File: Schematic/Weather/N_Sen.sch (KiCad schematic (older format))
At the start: 27 parts, among them J2 3_Way_Wire, J3 3_Way_Wire, Q1 BSS138, Q2 AO3401, Q3 AO3401, U5 LM321

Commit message: more changes
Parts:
- renumbered C4 to C1, H1 to H3, H2 to H4, H3 to H5, H4 to H6, J3 to J10, J2 to J9, R3 to R1, R12 to R10, R13 to R11, R14 to R12, R15 to R13, R16 to R14, R4 to R2, R5 to R3, R6 to R4, R7 to R5, R8 to R6, R9 to R7, R10 to R8, R11 to R9, U5 to U4
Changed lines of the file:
@@
 $Descr A4 11693 8268
 encoding utf-8
-Sheet 9 14
+Sheet 9 15
 Title ""
 Date ""
@@
 $EndComp
 $Comp
-L Amplifier_Operational:LM321 U5
+L Amplifier_Operational:LM321 U4
 U 1 1 5C8F90C7
 P 6050 2150
-F 0 "U5" H 6050 2631 50  0000 C CNN
+F 0 "U4" H 6050 2631 50  0000 C CNN
 F 1 "LM321" H 6050 2540 50  0000 C CNN
 F 2 "Package_TO_SOT_SMD:SOT-23-5" H 6050 2150 50  0001 C CNN
@@
 $EndComp
 $Comp
-L Device:R R3
+L Device:R R1
 U 1 1 5C90C2DD
 P 5450 4800
-F 0 "R3" V 5243 4800 50  0000 C CNN
+F 0 "R1" V 5243 4800 50  0000 C CNN
 F 1 "2.2K" V 5334 4800 50  0000 C CNN
 F 2 "Resistor_THT:R_Axial_DIN0204_L3.6mm_D1.6mm_P2.54mm_Vertical" V 5380 4800 50  0001 C CNN
@@
 $EndComp
 $Comp
-L Device:R R6
+L Device:R R4
 U 1 1 5C90E169
 P 5850 5250
-F 0 "R6" H 5780 5204 50  0000 R CNN
+F 0 "R4" H 5780 5204 50  0000 R CNN
 F 1 "5.1K" H 5780 5295 50  0000 R CNN
 F 2 "Resistor_THT:R_Axial_DIN0204_L3.6mm_D1.6mm_P2.54mm_Vertical" V 5780 5250 50  0001 C CNN
@@
 $EndComp
 $Comp
-L Device:R R14
+L Device:R R12
 U 1 1 5C90F143
 P 7350 4900
-F 0 "R14" H 7420 4946 50  0000 L CNN
+F 0 "R12" H 7420 4946 50  0000 L CNN
 F 1 "680" H 7420 4855 50  0000 L CNN
 F 2 "Resistor_THT:R_Axial_DIN0204_L3.6mm_D1.6mm_P2.54mm_Vertical" V 7280 4900 50  0001 C CNN
@@
 $EndComp
 $Comp
-L Device:R R12
+L Device:R R10
 U 1 1 5C9100FA
 P 7050 3900
-F 0 "R12" H 7120 3946 50  0000 L CNN
+F 0 "R10" H 7120 3946 50  0000 L CNN
 F 1 "20K" H 7120 3855 50  0000 L CNN
 F 2 "Resistor_THT:R_Axial_DIN0204_L3.6mm_D1.6mm_P2.54mm_Vertical" V 6980 3900 50  0001 C CNN
@@
 $EndComp
 $Comp
-L Device:R R8
+L Device:R R6
 U 1 1 5C913744
 P 6300 4150
-F 0 "R8" H 6370 4196 50  0000 L CNN
+F 0 "R6" H 6370 4196 50  0000 L CNN
 F 1 "10K" H 6370 4105 50  0000 L CNN
 F 2 "Resistor_THT:R_Axial_DIN0204_L3.6mm_D1.6mm_P2.54mm_Vertical" V 6230 4150 50  0001 C CNN
@@
 $EndComp
 $Comp
-L Device:R R5
+L Device:R R3
 U 1 1 5C91429E
 P 5750 3700
-F 0 "R5" H 5820 3746 50  0000 L CNN
+F 0 "R3" H 5820 3746 50  0000 L CNN
 F 1 "2.2k" H 5820 3655 50  0000 L CNN
 F 2 "Resistor_THT:R_Axial_DIN0204_L3.6mm_D1.6mm_P2.54mm_Vertical" V 5680 3700 50  0001 C CNN
@@
 $EndComp
 $Comp
-L Device:R R9
+L Device:R R7
 U 1 1 5C919740
 P 6400 1700
-F 0 "R9" H 6470 1746 50  0000 L CNN
+F 0 "R7" H 6470 1746 50  0000 L CNN
 F 1 "4.7K" H 6470 1655 50  0000 L CNN
 F 2 "Resistor_THT:R_Axial_DIN0204_L3.6mm_D1.6mm_P2.54mm_Vertical" V 6330 1700 50  0001 C CNN
@@
 $EndComp
 $Comp
-L Device:R R4
+L Device:R R2
 U 1 1 5C902560
 P 5500 2150
-F 0 "R4" V 5293 2150 50  0000 C CNN
+F 0 "R2" V 5293 2150 50  0000 C CNN
 F 1 "4.7K" V 5384 2150 50  0000 C CNN
 F 2 "Resistor_THT:R_Axial_DIN0204_L3.6mm_D1.6mm_P2.54mm_Vertical" V 5430 2150 50  0001 C CNN
@@
 	7350 5650 7950 5650
 $Comp
-L Device:R R13
+L Device:R R11
 U 1 1 5C9120FF
 P 7050 4900
-F 0 "R13" H 7120 4946 50  0000 L CNN
+F 0 "R11" H 7120 4946 50  0000 L CNN
 F 1 "20K" H 7120 4855 50  0000 L CNN
 F 2 "Resistor_THT:R_Axial_DIN0204_L3.6mm_D1.6mm_P2.54mm_Vertical" V 6980 4900 50  0001 C CNN
@@
 	6150 1350 6150 1850
 $Comp
-L Device:R R16
+L Device:R R14
 U 1 1 5C914922
 P 7750 2250
-F 0 "R16" V 7543 2250 50  0000 C CNN
+F 0 "R14" V 7543 2250 50  0000 C CNN
 F 1 "3.3k" V 7634 2250 50  0000 C CNN
 F 2 "Resistor_THT:R_Axial_DIN0204_L3.6mm_D1.6mm_P2.54mm_Vertical" V 7680 2250 50  0001 C CNN
@@
 	7400 2550 7300 2550
 $Comp
-L Device:R R10
+L Device:R R8
 U 1 1 5C96EBEA
 P 6400 2650
-F 0 "R10" H 6470 2696 50  0000 L CNN
+F 0 "R8" H 6470 2696 50  0000 L CNN
 F 1 "4.7K" H 6470 2605 50  0000 L CNN
 F 2 "Resistor_THT:R_Axial_DIN0204_L3.6mm_D1.6mm_P2.54mm_Vertical" V 6330 2650 50  0001 C CNN
@@
 Connection ~ 7400 2250
 $Comp
-L Device:C C4
+L Device:C C1
 U 1 1 5C96A149
 P 6900 2250
-F 0 "C4" V 6648 2250 50  0000 C CNN
+F 0 "C1" V 6648 2250 50  0000 C CNN
 F 1 "0.1uF" V 6739 2250 50  0000 C CNN
 F 2 "Capacitor_THT:C_Disc_D3.8mm_W2.6mm_P2.50mm" H 6938 2100 50  0001 C CNN
@@
 24v
 $Comp
-L Device:R R11
+L Device:R R9
 U 1 1 5C96E23C
 P 6600 2250
-F 0 "R11" V 6393 2250 50  0000 C CNN
+F 0 "R9" V 6393 2250 50  0000 C CNN
 F 1 "4.7K" V 6484 2250 50  0000 C CNN
 F 2 "Resistor_THT:R_Axial_DIN0204_L3.6mm_D1.6mm_P2.54mm_Vertical" V 6530 2250 50  0001 C CNN
@@
 Connection ~ 6400 2850
 $Comp
-L Device:R R7
+L Device:R R5
 U 1 1 5C97DE0F
 P 5900 2500
-F 0 "R7" V 5693 2500 50  0000 C CNN
+F 0 "R5" V 5693 2500 50  0000 C CNN
 F 1 "4.7K" V 5784 2500 50  0000 C CNN
 F 2 "Resistor_THT:R_Axial_DIN0204_L3.6mm_D1.6mm_P2.54mm_Vertical" V 5830 2500 50  0001 C CNN
@@
 	7700 3450 7700 3650
 $Comp
-L Device:R R15
+L Device:R R13
 U 1 1 5C912BAF
 P 7700 3800
-F 0 "R15" H 7770 3846 50  0000 L CNN
+F 0 "R13" H 7770 3846 50  0000 L CNN
 F 1 "47K" H 7770 3755 50  0000 L CNN
 F 2 "Resistor_THT:R_Axial_DIN0204_L3.6mm_D1.6mm_P2.54mm_Vertical" V 7630 3800 50  0001 C CNN
@@
 	4750 1350 6150 1350
 $Comp
-L MyComponents:3_Way_Wire J3
+L MyComponents:3_Way_Wire J10
 U 1 1 5C9F0115
 P 3650 2000
-F 0 "J3" H 3500 1600 50  0000 L CNN
+F 0 "J10" H 3500 1600 50  0000 L CNN
 F 1 "3_Way_Wire" H 3450 1450 50  0000 L CNN
 F 2 "Connector_PinHeader_2.54mm:PinHeader_1x03_P2.54mm_Vertical" H 3650 2000 50  0001 C CNN
@@
 Connection ~ 4600 2850
 $Comp
-L MyComponents:3_Way_Wire J2
+L MyComponents:3_Way_Wire J9
 U 1 1 5C9F0A63
 P 3600 3350
-F 0 "J2" H 3500 2950 50  0000 L CNN
+F 0 "J9" H 3500 2950 50  0000 L CNN
 F 1 "3_Way_Wire" H 3450 2800 50  0000 L CNN
 F 2 "Connector_PinHeader_2.54mm:PinHeader_1x03_P2.54mm_Vertical" H 3600 3350 50  0001 C CNN
@@
 Connection ~ 5750 3450
 $Comp
-L Mechanical:MountingHole_Pad H1
+L Mechanical:MountingHole_Pad H3
 U 1 1 5CA34377
 P 8350 3350
-F 0 "H1" H 8450 3399 50  0000 L CNN
+F 0 "H3" H 8450 3399 50  0000 L CNN
 F 1 "MountingHole_Pad" H 8450 3308 50  0000 L CNN
 F 2 "Connector_Wire:SolderWirePad_1x01_Drill0.8mm" H 8350 3350 50  0001 C CNN
@@
 $EndComp
 $Comp
-L Mechanical:MountingHole_Pad H3
+L Mechanical:MountingHole_Pad H5
 U 1 1 5CA34DBD
 P 8350 3850
-F 0 "H3" H 8450 3899 50  0000 L CNN
+F 0 "H5" H 8450 3899 50  0000 L CNN
 F 1 "MountingHole_Pad" H 8450 3808 50  0000 L CNN
 F 2 "Connector_Wire:SolderWirePad_1x01_Drill0.8mm" H 8350 3850 50  0001 C CNN
@@
 $EndComp
 $Comp
-L Mechanical:MountingHole_Pad H2
+L Mechanical:MountingHole_Pad H4
 U 1 1 5CA4F9CF
 P 8350 3550
-F 0 "H2" H 8250 3507 50  0000 R CNN
+F 0 "H4" H 8250 3507 50  0000 R CNN
 F 1 "MountingHole_Pad" H 8250 3598 50  0000 R CNN
 F 2 "Connector_Wire:SolderWirePad_1x01_Drill0.8mm" H 8350 3550 50  0001 C CNN
@@
 Connection ~ 8350 3450
 $Comp
-L Mechanical:MountingHole_Pad H4
+L Mechanical:MountingHole_Pad H6
 U 1 1 5CA5112A
 P 8350 4050
-F 0 "H4" H 8250 4007 50  0000 R CNN
+F 0 "H6" H 8250 4007 50  0000 R CNN
 F 1 "MountingHole_Pad" H 8250 4098 50  0000 R CNN
 F 2 "Connector_Wire:SolderWirePad_1x01_Drill0.8mm" H 8350 4050 50  0001 C CNN

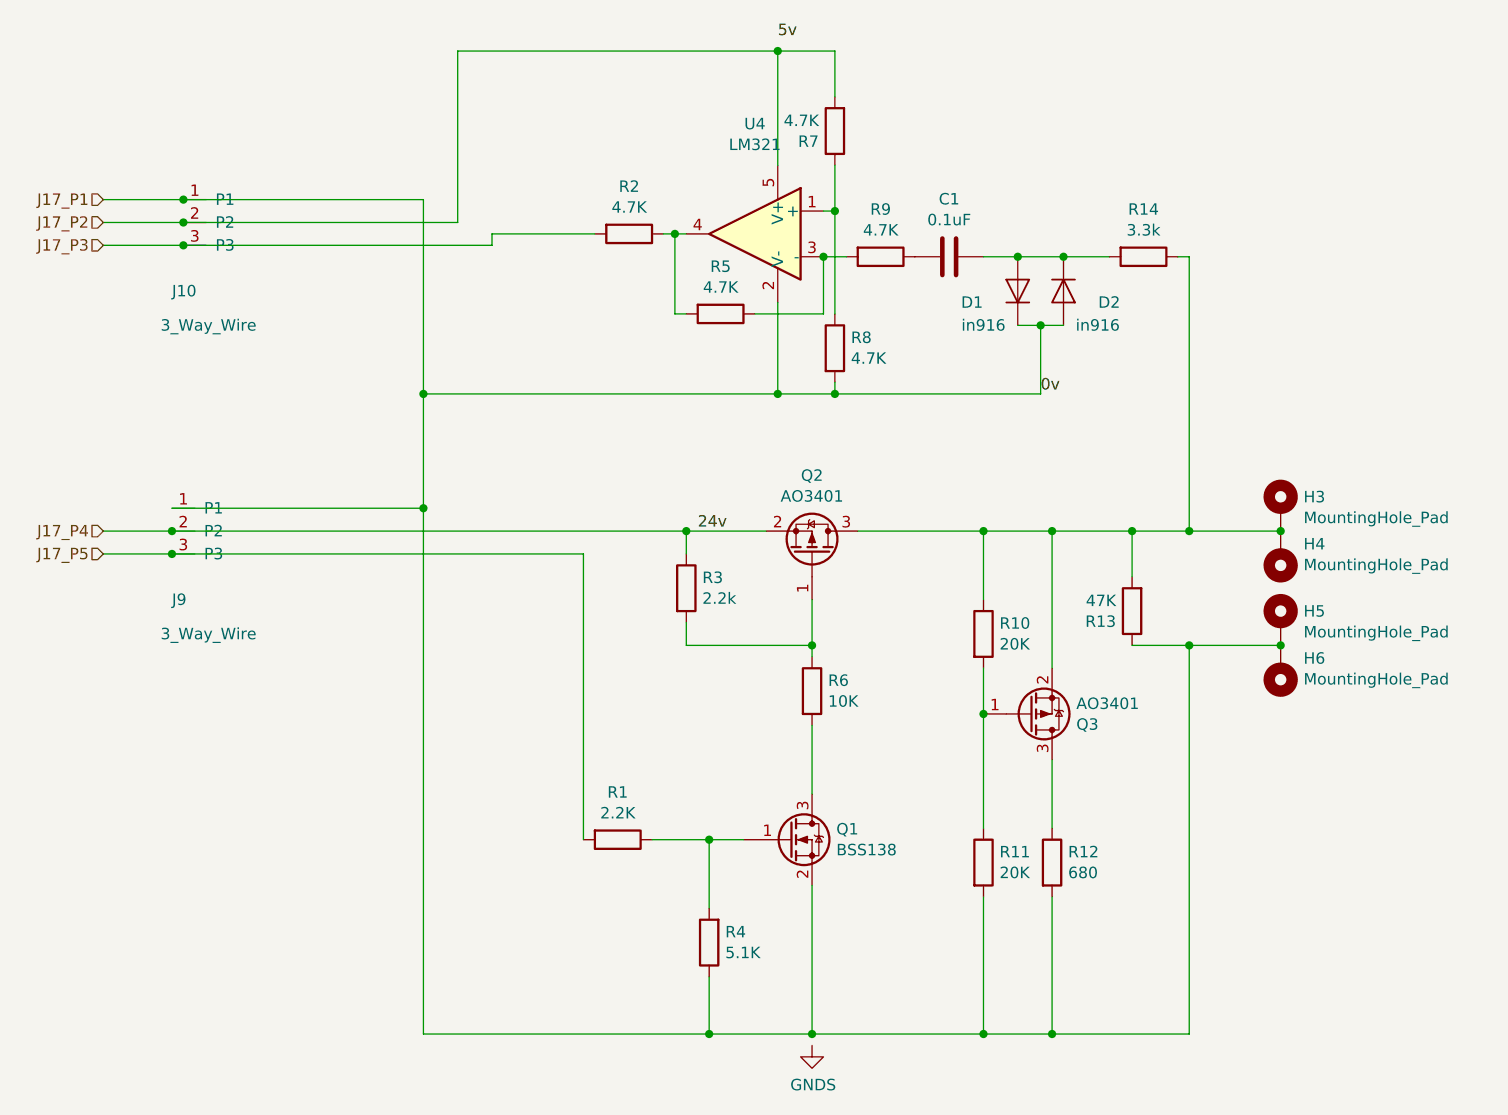
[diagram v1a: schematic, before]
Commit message: Connector relable start
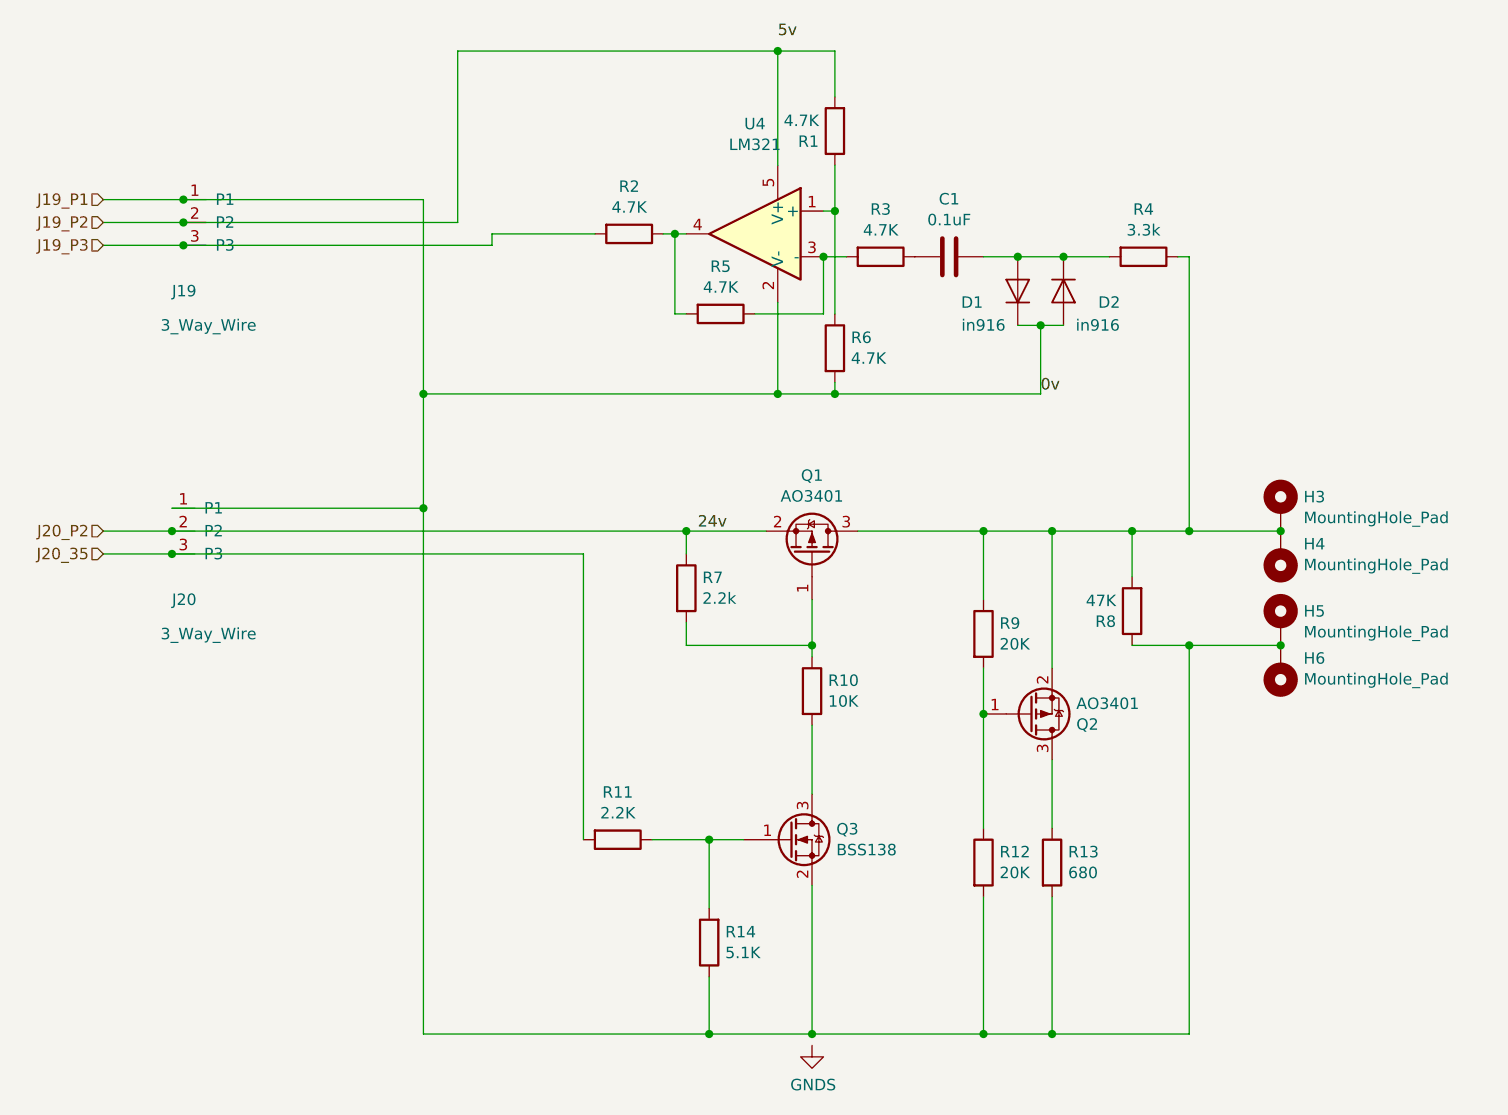
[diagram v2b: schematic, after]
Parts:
- renumbered J10 to J19, J9 to J20, Q2 to Q1, Q3 to Q2, Q1 to Q3, R7 to R1, R6 to R10, R1 to R11, R11 to R12, R12 to R13, R4 to R14, R9 to R3, R14 to R4, R8 to R6, R3 to R7, R13 to R8, R10 to R9
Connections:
- net J17_P1 renamed J19_P1
- net J17_P2 renamed J19_P2
- net J17_P3 renamed J19_P3
- net J17_P4 renamed J20_P2
- net J17_P5 renamed J20_35
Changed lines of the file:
@@
 $Descr A4 11693 8268
 encoding utf-8
-Sheet 9 15
+Sheet 7 15
 Title ""
 Date ""
@@
 $EndDescr
 Text HLabel 3200 2000 0    50   Input ~ 0
-J17_P1
+J19_P1
 Text HLabel 3200 2100 0    50   Input ~ 0
-J17_P2
+J19_P2
 Text HLabel 3200 2200 0    50   Input ~ 0
-J17_P3
+J19_P3
 Text HLabel 3200 3450 0    50   Input ~ 0
-J17_P4
-$Comp
-L Weather-rescue:AO3401-Transistor_FET Q2
+J20_P2
+$Comp
+L Weather-rescue:AO3401-Transistor_FET Q1
 U 1 1 5C8F913C
 P 6300 3550
-F 0 "Q2" V 6643 3550 50  0000 C CNN
+F 0 "Q1" V 6643 3550 50  0000 C CNN
 F 1 "AO3401" V 6552 3550 50  0000 C CNN
 F 2 "Package_TO_SOT_SMD:SOT-23" H 6500 3475 50  0001 L CIN
@@
 $EndComp
 $Comp
-L Transistor_FET:BSS138 Q1
+L Transistor_FET:BSS138 Q3
 U 1 1 5C904FFF
 P 6200 4800
-F 0 "Q1" H 6406 4846 50  0000 L CNN
+F 0 "Q3" H 6406 4846 50  0000 L CNN
 F 1 "BSS138" H 6406 4755 50  0000 L CNN
 F 2 "Package_TO_SOT_SMD:SOT-23" H 6400 4725 50  0001 L CIN
@@
 $EndComp
 $Comp
-L Device:R R1
+L Device:R R11
 U 1 1 5C90C2DD
 P 5450 4800
-F 0 "R1" V 5243 4800 50  0000 C CNN
+F 0 "R11" V 5243 4800 50  0000 C CNN
 F 1 "2.2K" V 5334 4800 50  0000 C CNN
 F 2 "Resistor_THT:R_Axial_DIN0204_L3.6mm_D1.6mm_P2.54mm_Vertical" V 5380 4800 50  0001 C CNN
@@
 $EndComp
 $Comp
-L Device:R R4
+L Device:R R14
 U 1 1 5C90E169
 P 5850 5250
-F 0 "R4" H 5780 5204 50  0000 R CNN
+F 0 "R14" H 5780 5204 50  0000 R CNN
 F 1 "5.1K" H 5780 5295 50  0000 R CNN
 F 2 "Resistor_THT:R_Axial_DIN0204_L3.6mm_D1.6mm_P2.54mm_Vertical" V 5780 5250 50  0001 C CNN
@@
 $EndComp
 $Comp
-L Device:R R12
+L Device:R R13
 U 1 1 5C90F143
 P 7350 4900
-F 0 "R12" H 7420 4946 50  0000 L CNN
+F 0 "R13" H 7420 4946 50  0000 L CNN
 F 1 "680" H 7420 4855 50  0000 L CNN
 F 2 "Resistor_THT:R_Axial_DIN0204_L3.6mm_D1.6mm_P2.54mm_Vertical" V 7280 4900 50  0001 C CNN
@@
 $EndComp
 $Comp
-L Device:R R10
+L Device:R R9
 U 1 1 5C9100FA
 P 7050 3900
-F 0 "R10" H 7120 3946 50  0000 L CNN
+F 0 "R9" H 7120 3946 50  0000 L CNN
 F 1 "20K" H 7120 3855 50  0000 L CNN
 F 2 "Resistor_THT:R_Axial_DIN0204_L3.6mm_D1.6mm_P2.54mm_Vertical" V 6980 3900 50  0001 C CNN
@@
 $EndComp
 $Comp
-L Device:R R6
+L Device:R R10
 U 1 1 5C913744
 P 6300 4150
-F 0 "R6" H 6370 4196 50  0000 L CNN
+F 0 "R10" H 6370 4196 50  0000 L CNN
 F 1 "10K" H 6370 4105 50  0000 L CNN
 F 2 "Resistor_THT:R_Axial_DIN0204_L3.6mm_D1.6mm_P2.54mm_Vertical" V 6230 4150 50  0001 C CNN
@@
 $EndComp
 $Comp
-L Device:R R3
+L Device:R R7
 U 1 1 5C91429E
 P 5750 3700
-F 0 "R3" H 5820 3746 50  0000 L CNN
+F 0 "R7" H 5820 3746 50  0000 L CNN
 F 1 "2.2k" H 5820 3655 50  0000 L CNN
 F 2 "Resistor_THT:R_Axial_DIN0204_L3.6mm_D1.6mm_P2.54mm_Vertical" V 5680 3700 50  0001 C CNN
@@
 $EndComp
 $Comp
-L Device:R R7
+L Device:R R1
 U 1 1 5C919740
 P 6400 1700
-F 0 "R7" H 6470 1746 50  0000 L CNN
+F 0 "R1" H 6470 1746 50  0000 L CNN
 F 1 "4.7K" H 6470 1655 50  0000 L CNN
 F 2 "Resistor_THT:R_Axial_DIN0204_L3.6mm_D1.6mm_P2.54mm_Vertical" V 6330 1700 50  0001 C CNN
@@
 	6500 3450 7050 3450
 $Comp
-L Weather-rescue:AO3401-Transistor_FET Q3
+L Weather-rescue:AO3401-Transistor_FET Q2
 U 1 1 5C900ECB
 P 7250 4250
-F 0 "Q3" H 7456 4296 50  0000 L CNN
+F 0 "Q2" H 7456 4296 50  0000 L CNN
 F 1 "AO3401" H 7456 4205 50  0000 L CNN
 F 2 "Package_TO_SOT_SMD:SOT-23" H 7450 4175 50  0001 L CIN
@@
 	7350 5650 7950 5650
 $Comp
-L Device:R R11
+L Device:R R12
 U 1 1 5C9120FF
 P 7050 4900
-F 0 "R11" H 7120 4946 50  0000 L CNN
+F 0 "R12" H 7120 4946 50  0000 L CNN
 F 1 "20K" H 7120 4855 50  0000 L CNN
 F 2 "Resistor_THT:R_Axial_DIN0204_L3.6mm_D1.6mm_P2.54mm_Vertical" V 6980 4900 50  0001 C CNN
@@
 	6150 1350 6150 1850
 $Comp
-L Device:R R14
+L Device:R R4
 U 1 1 5C914922
 P 7750 2250
-F 0 "R14" V 7543 2250 50  0000 C CNN
+F 0 "R4" V 7543 2250 50  0000 C CNN
 F 1 "3.3k" V 7634 2250 50  0000 C CNN
 F 2 "Resistor_THT:R_Axial_DIN0204_L3.6mm_D1.6mm_P2.54mm_Vertical" V 7680 2250 50  0001 C CNN
@@
 	7400 2550 7300 2550
 $Comp
-L Device:R R8
+L Device:R R6
 U 1 1 5C96EBEA
 P 6400 2650
-F 0 "R8" H 6470 2696 50  0000 L CNN
+F 0 "R6" H 6470 2696 50  0000 L CNN
 F 1 "4.7K" H 6470 2605 50  0000 L CNN
 F 2 "Resistor_THT:R_Axial_DIN0204_L3.6mm_D1.6mm_P2.54mm_Vertical" V 6330 2650 50  0001 C CNN
@@
 24v
 $Comp
-L Device:R R9
+L Device:R R3
 U 1 1 5C96E23C
 P 6600 2250
-F 0 "R9" V 6393 2250 50  0000 C CNN
+F 0 "R3" V 6393 2250 50  0000 C CNN
 F 1 "4.7K" V 6484 2250 50  0000 C CNN
 F 2 "Resistor_THT:R_Axial_DIN0204_L3.6mm_D1.6mm_P2.54mm_Vertical" V 6530 2250 50  0001 C CNN
@@
 Connection ~ 6350 2250
 Text HLabel 3200 3550 0    50   Input ~ 0
-J17_P5
+J20_35
 Wire Wire Line
 	5750 3850 5750 3950
@@
 	7700 3450 7700 3650
 $Comp
-L Device:R R13
+L Device:R R8
 U 1 1 5C912BAF
 P 7700 3800
-F 0 "R13" H 7770 3846 50  0000 L CNN
+F 0 "R8" H 7770 3846 50  0000 L CNN
 F 1 "47K" H 7770 3755 50  0000 L CNN
 F 2 "Resistor_THT:R_Axial_DIN0204_L3.6mm_D1.6mm_P2.54mm_Vertical" V 7630 3800 50  0001 C CNN
@@
 	4750 1350 6150 1350
 $Comp
-L MyComponents:3_Way_Wire J10
+L MyComponents:3_Way_Wire J19
 U 1 1 5C9F0115
 P 3650 2000
-F 0 "J10" H 3500 1600 50  0000 L CNN
+F 0 "J19" H 3500 1600 50  0000 L CNN
 F 1 "3_Way_Wire" H 3450 1450 50  0000 L CNN
 F 2 "Connector_PinHeader_2.54mm:PinHeader_1x03_P2.54mm_Vertical" H 3650 2000 50  0001 C CNN
@@
 Connection ~ 4600 2850
 $Comp
-L MyComponents:3_Way_Wire J9
+L MyComponents:3_Way_Wire J20
 U 1 1 5C9F0A63
 P 3600 3350
-F 0 "J9" H 3500 2950 50  0000 L CNN
+F 0 "J20" H 3500 2950 50  0000 L CNN
 F 1 "3_Way_Wire" H 3450 2800 50  0000 L CNN
 F 2 "Connector_PinHeader_2.54mm:PinHeader_1x03_P2.54mm_Vertical" H 3600 3350 50  0001 C CNN
